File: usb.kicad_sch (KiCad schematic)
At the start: 9 parts

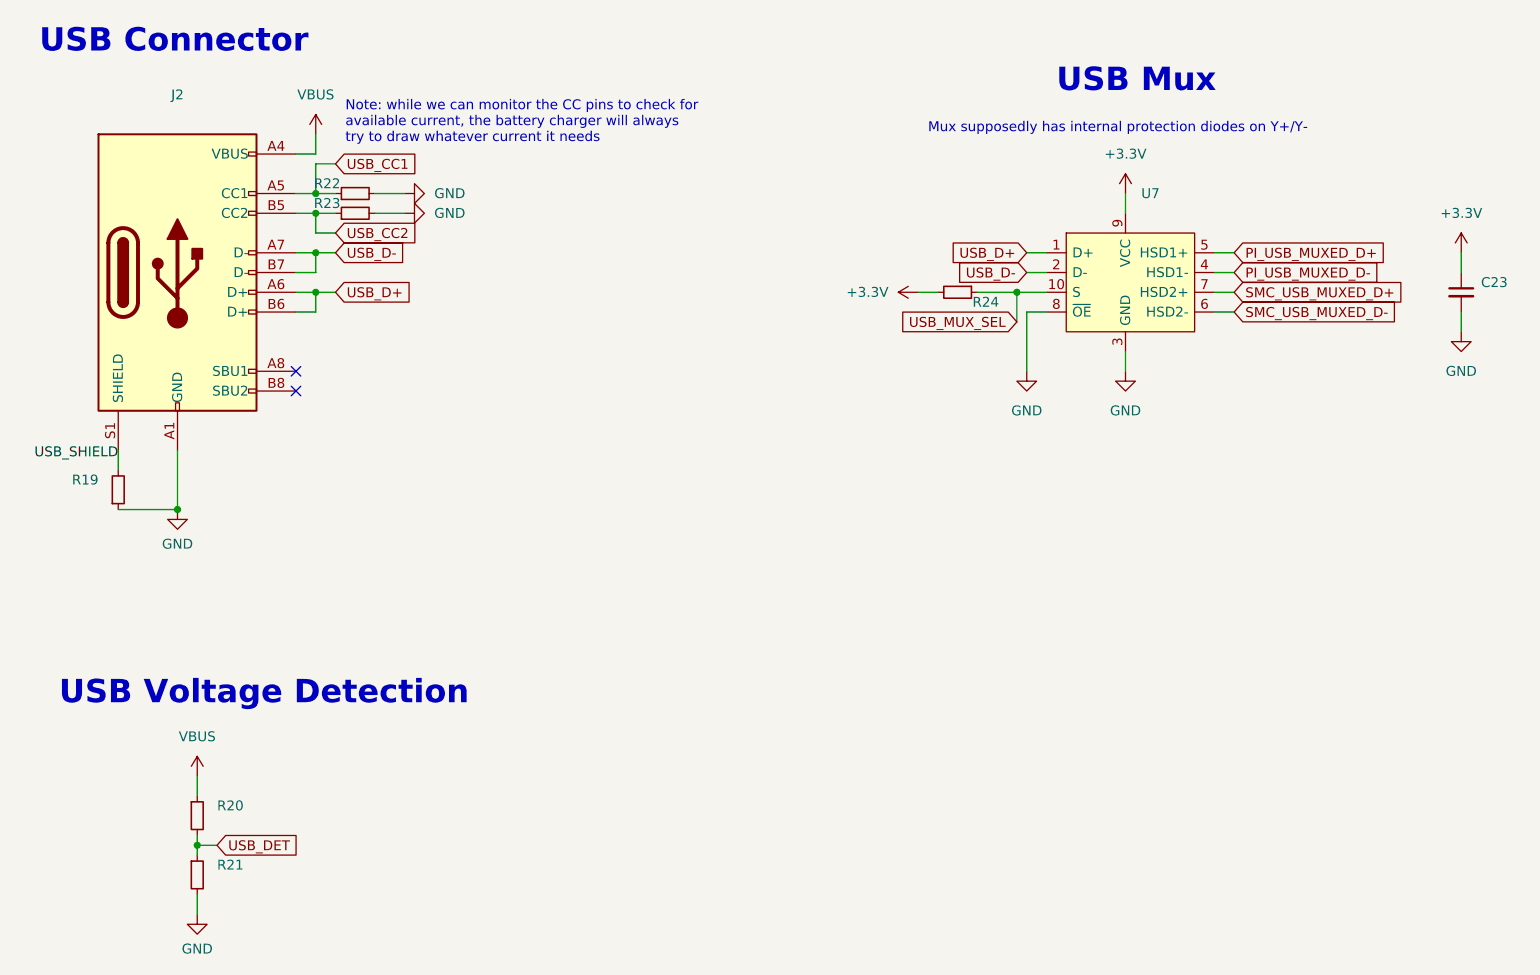
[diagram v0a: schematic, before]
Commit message: layout: add testpoints, extra mounting hole, grounding clips
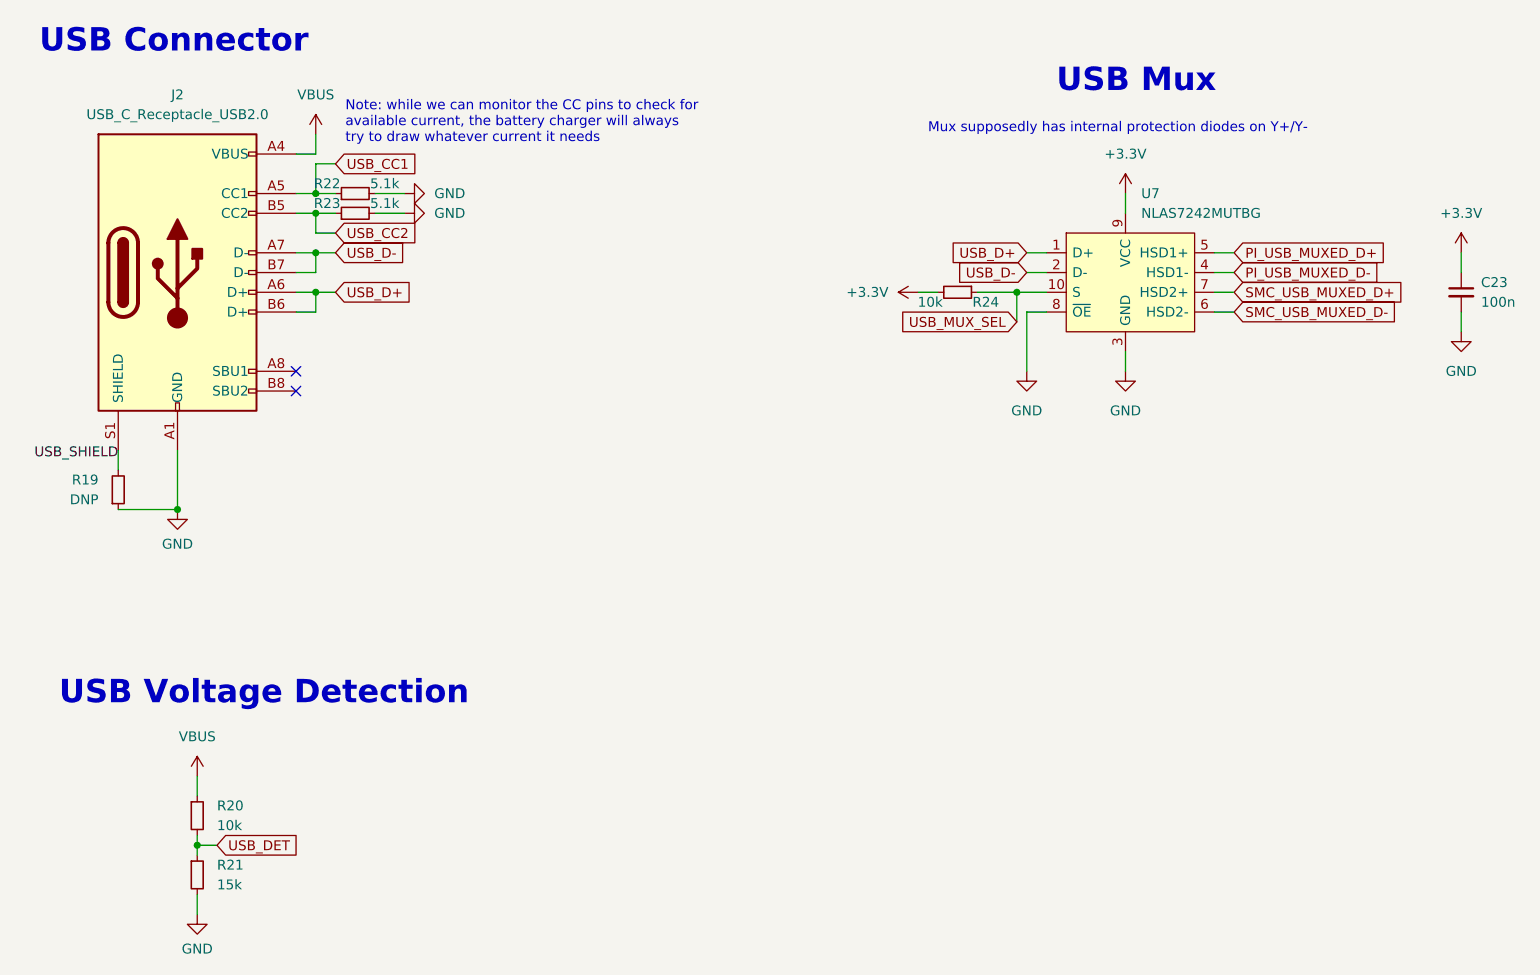
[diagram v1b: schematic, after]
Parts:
- C23: value (none) -> 100n; footprint (none) -> Capacitor_SMD:C_0402_1005Metric
- J2: value (none) -> USB_C_Receptacle_USB2.0; footprint (none) -> Gigahawk:USB_C_Receptacle_GCT_USB4085
- R19: value (none) -> DNP; footprint (none) -> Resistor_SMD:R_0402_1005Metric
- R20, R24: value (none) -> 10k; footprint (none) -> Resistor_SMD:R_0402_1005Metric
- R21: value (none) -> 15k; footprint (none) -> Resistor_SMD:R_0402_1005Metric
- R22, R23: value (none) -> 5.1k; footprint (none) -> Resistor_SMD:R_0402_1005Metric
- U7: value (none) -> NLAS7242MUTBG; footprint (none) -> Package_DFN_QFN:UQFN-10_1.4x1.8mm_P0.4mm
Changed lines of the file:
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@@
       (effects (font (size 1.27 1.27)) (justify left))
     )
-    (property "Value" "" (id 1) (at 68.58 158.7499 0)
-      (effects (font (size 1.27 1.27)) (justify left))
-    )
-    (property "Footprint" "" (id 2) (at 66.04 157.48 0)
+    (property "Value" "15k" (id 1) (at 68.58 158.7499 0)
+      (effects (font (size 1.27 1.27)) (justify left))
+    )
+    (property "Footprint" "Resistor_SMD:R_0402_1005Metric" (id 2) (at 66.04 157.48 0)
       (effects (font (size 1.27 1.27)) hide)
     )
@@
       (effects (font (size 1.27 1.27)) (justify left))
     )
-    (property "Value" "" (id 1) (at 161.925 83.82 90)
-      (effects (font (size 1.27 1.27)) (justify right))
-    )
-    (property "Footprint" "" (id 2) (at 163.83 82.55 0)
+    (property "Value" "10k" (id 1) (at 161.925 83.82 90)
+      (effects (font (size 1.27 1.27)) (justify right))
+    )
+    (property "Footprint" "Resistor_SMD:R_0402_1005Metric" (id 2) (at 163.83 82.55 0)
       (effects (font (size 1.27 1.27)) hide)
     )
@@
       (effects (font (size 1.27 1.27)) (justify left))
     )
-    (property "Value" "" (id 1) (at 68.58 151.1299 0)
-      (effects (font (size 1.27 1.27)) (justify left))
-    )
-    (property "Footprint" "" (id 2) (at 66.04 149.86 0)
+    (property "Value" "10k" (id 1) (at 68.58 151.1299 0)
+      (effects (font (size 1.27 1.27)) (justify left))
+    )
+    (property "Footprint" "Resistor_SMD:R_0402_1005Metric" (id 2) (at 66.04 149.86 0)
       (effects (font (size 1.27 1.27)) hide)
     )
@@
       (effects (font (size 1.27 1.27)) (justify left))
     )
-    (property "Value" "" (id 1) (at 88.265 68.58 90)
-      (effects (font (size 1.27 1.27)) (justify right))
-    )
-    (property "Footprint" "" (id 2) (at 86.36 69.85 0)
+    (property "Value" "5.1k" (id 1) (at 88.265 68.58 90)
+      (effects (font (size 1.27 1.27)) (justify right))
+    )
+    (property "Footprint" "Resistor_SMD:R_0402_1005Metric" (id 2) (at 86.36 69.85 0)
       (effects (font (size 1.27 1.27)) hide)
     )
@@
       (effects (font (size 1.27 1.27)) (justify left))
     )
-    (property "Value" "" (id 1) (at 187.4394 72.39 0)
-      (effects (font (size 1.27 1.27)) (justify left))
-    )
-    (property "Footprint" "" (id 2) (at 167.64 64.77 0)
+    (property "Value" "NLAS7242MUTBG" (id 1) (at 187.4394 72.39 0)
+      (effects (font (size 1.27 1.27)) (justify left))
+    )
+    (property "Footprint" "Package_DFN_QFN:UQFN-10_1.4x1.8mm_P0.4mm" (id 2) (at 167.64 64.77 0)
       (effects (font (size 1.27 1.27)) (justify left) hide)
     )
@@
       (effects (font (size 1.27 1.27)) (justify left))
     )
-    (property "Value" "" (id 1) (at 231.14 83.8262 0)
-      (effects (font (size 1.27 1.27)) (justify left))
-    )
-    (property "Footprint" "" (id 2) (at 228.6 82.55 0)
+    (property "Value" "100n" (id 1) (at 231.14 83.8262 0)
+      (effects (font (size 1.27 1.27)) (justify left))
+    )
+    (property "Footprint" "Capacitor_SMD:C_0402_1005Metric" (id 2) (at 228.6 82.55 0)
       (effects (font (size 1.27 1.27)) hide)
     )
@@
       (effects (font (size 1.27 1.27)) (justify left))
     )
-    (property "Value" "" (id 1) (at 88.265 71.12 90)
-      (effects (font (size 1.27 1.27)) (justify right))
-    )
-    (property "Footprint" "" (id 2) (at 86.36 72.39 0)
+    (property "Value" "5.1k" (id 1) (at 88.265 71.12 90)
+      (effects (font (size 1.27 1.27)) (justify right))
+    )
+    (property "Footprint" "Resistor_SMD:R_0402_1005Metric" (id 2) (at 86.36 72.39 0)
       (effects (font (size 1.27 1.27)) hide)
     )
@@
     (in_bom yes) (on_board yes) (fields_autoplaced)
     (property "Reference" "J2" (id 0) (at 63.5 57.15 0))
-    (property "Value" "" (id 1) (at 63.5 59.69 0))
-    (property "Footprint" "" (id 2) (at 67.31 80.01 0)
+    (property "Value" "USB_C_Receptacle_USB2.0" (id 1) (at 63.5 59.69 0))
+    (property "Footprint" "Gigahawk:USB_C_Receptacle_GCT_USB4085" (id 2) (at 67.31 80.01 0)
       (effects (font (size 1.27 1.27)) hide)
     )
@@
       (effects (font (size 1.27 1.27)) (justify right))
     )
-    (property "Value" "" (id 1) (at 53.34 109.2199 0)
-      (effects (font (size 1.27 1.27)) (justify right))
-    )
-    (property "Footprint" "" (id 2) (at 55.88 107.95 0)
-      (effects (font (size 1.27 1.27)) hide)
-    )
+    (property "Value" "DNP" (id 1) (at 53.34 109.2199 0)
+      (effects (font (size 1.27 1.27)) (justify right))
+    )
+    (property "Footprint" "Resistor_SMD:R_0402_1005Metric" (id 2) (at 55.88 107.95 0)
+      (effects (font (size 1.27 1.27)) hide)
+    )

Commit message: ci: prepare files for CI
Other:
- title: (none) -> piPod IO/SMC Board
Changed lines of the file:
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@@
 (kicad_sch (version 20211123) (generator eeschema)
   (paper "A4")
+  (title_block
+    (title "piPod IO/SMC Board")
+    (date "${DATE}")
+    (rev "%{TAG} (${REVISION})")
+  )
   (junction (at 81.28 82.55) (diameter 0) (color 0 0 0 0)
   )

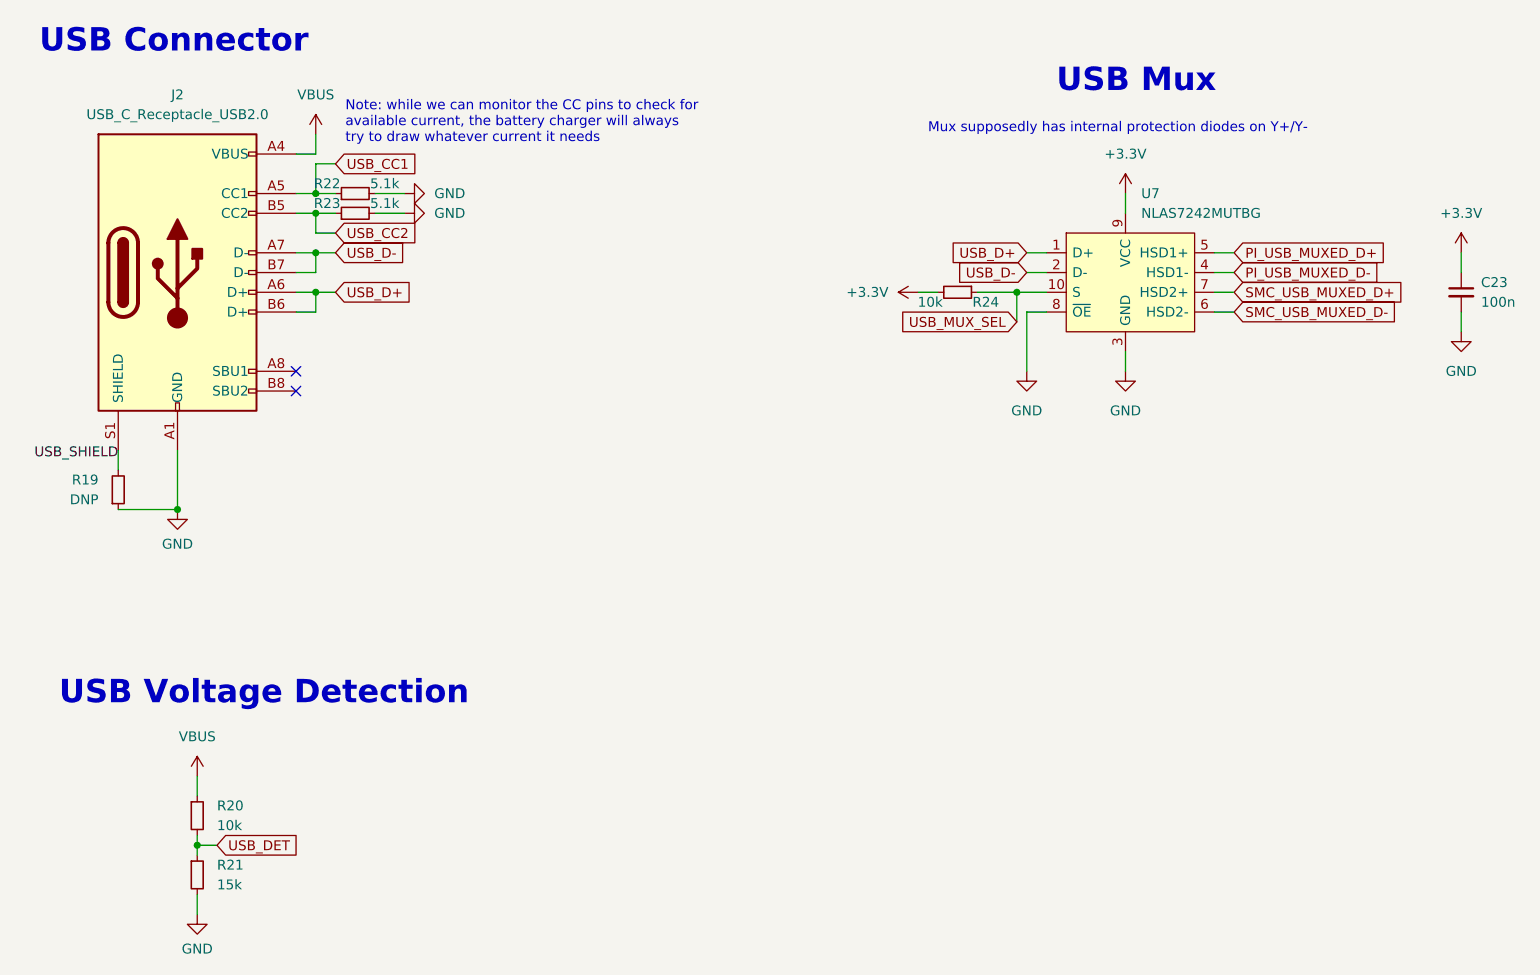
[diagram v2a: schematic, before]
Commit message: ci: test marking parts in sch for bom
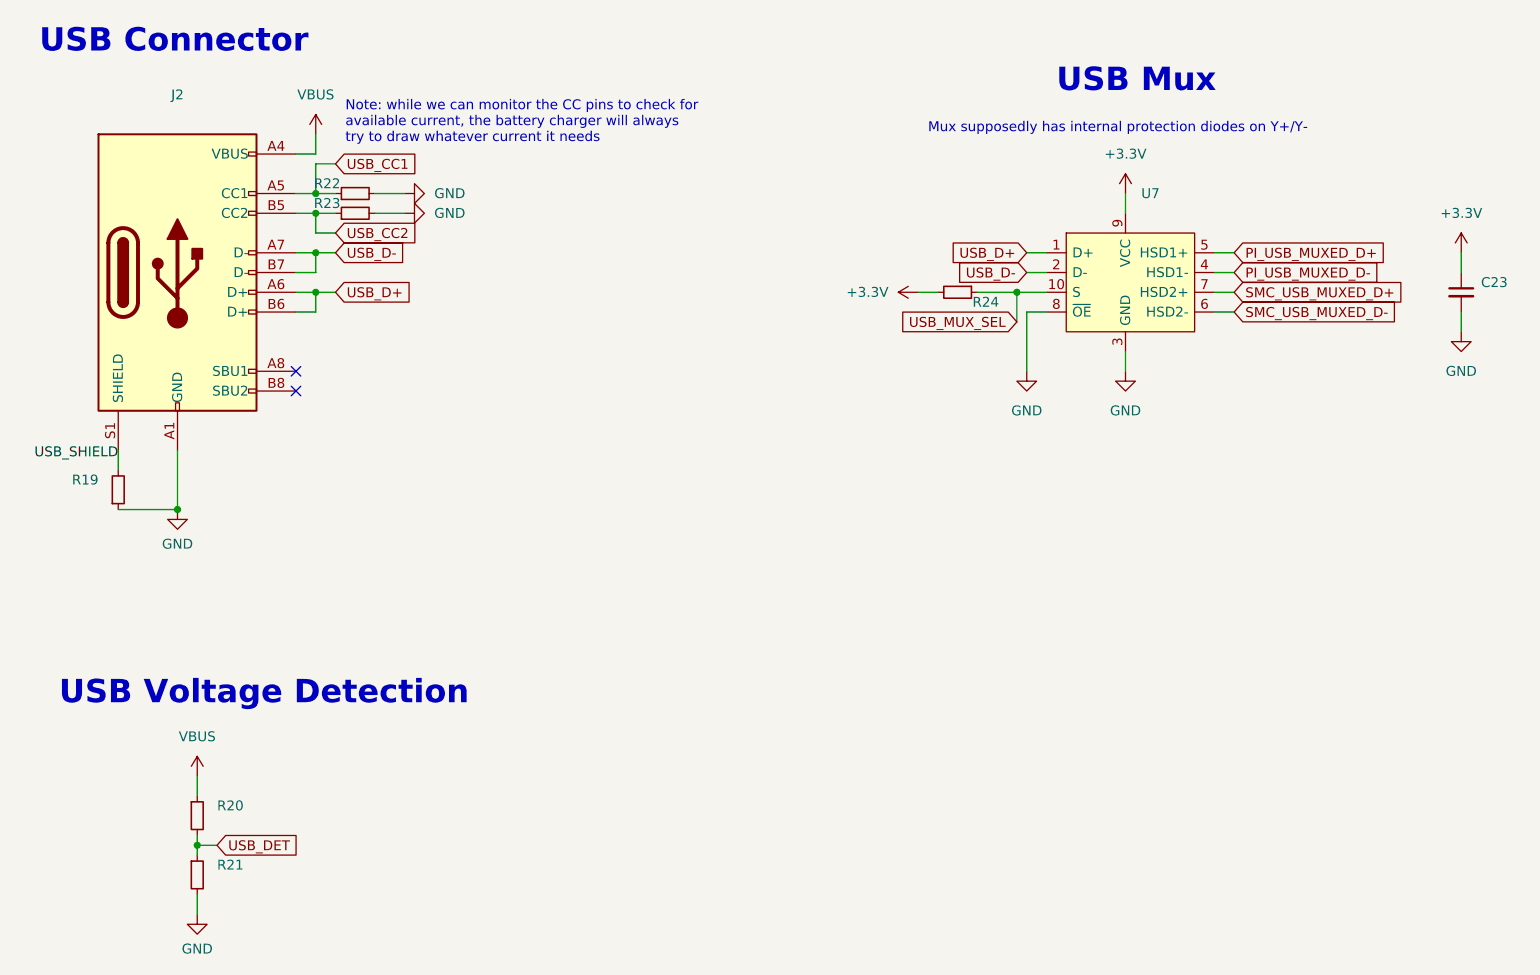
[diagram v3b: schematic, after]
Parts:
- C23: value 100n -> (none); footprint Capacitor_SMD:C_0402_1005Metric -> (none)
- J2: value USB_C_Receptacle_USB2.0 -> (none); footprint Gigahawk:USB_C_Receptacle_GCT_USB4085 -> (none)
- R19: value DNP -> (none); footprint Resistor_SMD:R_0402_1005Metric -> (none)
- R20, R24: value 10k -> (none); footprint Resistor_SMD:R_0402_1005Metric -> (none)
- R21: value 15k -> (none); footprint Resistor_SMD:R_0402_1005Metric -> (none)
- R22, R23: value 5.1k -> (none); footprint Resistor_SMD:R_0402_1005Metric -> (none)
- U7: value NLAS7242MUTBG -> (none); footprint Package_DFN_QFN:UQFN-10_1.4x1.8mm_P0.4mm -> (none)
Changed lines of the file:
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@@
       (effects (font (size 1.27 1.27)) (justify left))
     )
-    (property "Value" "15k" (id 1) (at 68.58 158.7499 0)
-      (effects (font (size 1.27 1.27)) (justify left))
-    )
-    (property "Footprint" "Resistor_SMD:R_0402_1005Metric" (id 2) (at 66.04 157.48 0)
+    (property "Value" "" (id 1) (at 68.58 158.7499 0)
+      (effects (font (size 1.27 1.27)) (justify left))
+    )
+    (property "Footprint" "" (id 2) (at 66.04 157.48 0)
       (effects (font (size 1.27 1.27)) hide)
     )
@@
       (effects (font (size 1.27 1.27)) (justify left))
     )
-    (property "Value" "10k" (id 1) (at 161.925 83.82 90)
-      (effects (font (size 1.27 1.27)) (justify right))
-    )
-    (property "Footprint" "Resistor_SMD:R_0402_1005Metric" (id 2) (at 163.83 82.55 0)
+    (property "Value" "" (id 1) (at 161.925 83.82 90)
+      (effects (font (size 1.27 1.27)) (justify right))
+    )
+    (property "Footprint" "" (id 2) (at 163.83 82.55 0)
       (effects (font (size 1.27 1.27)) hide)
     )
@@
       (effects (font (size 1.27 1.27)) (justify left))
     )
-    (property "Value" "10k" (id 1) (at 68.58 151.1299 0)
-      (effects (font (size 1.27 1.27)) (justify left))
-    )
-    (property "Footprint" "Resistor_SMD:R_0402_1005Metric" (id 2) (at 66.04 149.86 0)
+    (property "Value" "" (id 1) (at 68.58 151.1299 0)
+      (effects (font (size 1.27 1.27)) (justify left))
+    )
+    (property "Footprint" "" (id 2) (at 66.04 149.86 0)
       (effects (font (size 1.27 1.27)) hide)
     )
@@
       (effects (font (size 1.27 1.27)) (justify left))
     )
-    (property "Value" "5.1k" (id 1) (at 88.265 68.58 90)
-      (effects (font (size 1.27 1.27)) (justify right))
-    )
-    (property "Footprint" "Resistor_SMD:R_0402_1005Metric" (id 2) (at 86.36 69.85 0)
+    (property "Value" "" (id 1) (at 88.265 68.58 90)
+      (effects (font (size 1.27 1.27)) (justify right))
+    )
+    (property "Footprint" "" (id 2) (at 86.36 69.85 0)
       (effects (font (size 1.27 1.27)) hide)
     )
@@
       (effects (font (size 1.27 1.27)) (justify left))
     )
-    (property "Value" "NLAS7242MUTBG" (id 1) (at 187.4394 72.39 0)
-      (effects (font (size 1.27 1.27)) (justify left))
-    )
-    (property "Footprint" "Package_DFN_QFN:UQFN-10_1.4x1.8mm_P0.4mm" (id 2) (at 167.64 64.77 0)
+    (property "Value" "" (id 1) (at 187.4394 72.39 0)
+      (effects (font (size 1.27 1.27)) (justify left))
+    )
+    (property "Footprint" "" (id 2) (at 167.64 64.77 0)
       (effects (font (size 1.27 1.27)) (justify left) hide)
     )
@@
       (effects (font (size 1.27 1.27)) (justify left))
     )
-    (property "Value" "100n" (id 1) (at 231.14 83.8262 0)
-      (effects (font (size 1.27 1.27)) (justify left))
-    )
-    (property "Footprint" "Capacitor_SMD:C_0402_1005Metric" (id 2) (at 228.6 82.55 0)
+    (property "Value" "" (id 1) (at 231.14 83.8262 0)
+      (effects (font (size 1.27 1.27)) (justify left))
+    )
+    (property "Footprint" "" (id 2) (at 228.6 82.55 0)
       (effects (font (size 1.27 1.27)) hide)
     )
@@
       (effects (font (size 1.27 1.27)) (justify left))
     )
-    (property "Value" "5.1k" (id 1) (at 88.265 71.12 90)
-      (effects (font (size 1.27 1.27)) (justify right))
-    )
-    (property "Footprint" "Resistor_SMD:R_0402_1005Metric" (id 2) (at 86.36 72.39 0)
+    (property "Value" "" (id 1) (at 88.265 71.12 90)
+      (effects (font (size 1.27 1.27)) (justify right))
+    )
+    (property "Footprint" "" (id 2) (at 86.36 72.39 0)
       (effects (font (size 1.27 1.27)) hide)
     )
@@
     (in_bom yes) (on_board yes) (fields_autoplaced)
     (property "Reference" "J2" (id 0) (at 63.5 57.15 0))
-    (property "Value" "USB_C_Receptacle_USB2.0" (id 1) (at 63.5 59.69 0))
-    (property "Footprint" "Gigahawk:USB_C_Receptacle_GCT_USB4085" (id 2) (at 67.31 80.01 0)
+    (property "Value" "" (id 1) (at 63.5 59.69 0))
+    (property "Footprint" "" (id 2) (at 67.31 80.01 0)
       (effects (font (size 1.27 1.27)) hide)
     )
@@
       (effects (font (size 1.27 1.27)) (justify right))
     )
-    (property "Value" "DNP" (id 1) (at 53.34 109.2199 0)
-      (effects (font (size 1.27 1.27)) (justify right))
-    )
-    (property "Footprint" "Resistor_SMD:R_0402_1005Metric" (id 2) (at 55.88 107.95 0)
-      (effects (font (size 1.27 1.27)) hide)
-    )
+    (property "Value" "" (id 1) (at 53.34 109.2199 0)
+      (effects (font (size 1.27 1.27)) (justify right))
+    )
+    (property "Footprint" "" (id 2) (at 55.88 107.95 0)
+      (effects (font (size 1.27 1.27)) hide)
+    )
